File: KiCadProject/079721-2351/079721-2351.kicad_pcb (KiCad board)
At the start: 2 copper layers, 159.3 x 154.2 mm, 241 parts, among them IC1 HC244, IC101 uPC177C, IC201 MP493, IC401 D151811-0360, IC402 IS157, IC501 D151821-0020, IC601 MP5273, IC602 4071, IC603 4069, J201 Connected, J44 Conn_02x11_0x13_Top_Bottom_Sh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, J601 Connected, J711 Empty, Q802 C945, T1 2SB1015B, T211 RN1006, T711 2CS2001, T712 2SD1415, T721 2CS2001, T722 2SD1415, T751 CE1A3Q, T761 CE1A3Q, T801 2CS2001, T803 2CS4065, T811 2SC1815, T812 CE1A3Q, T821 Empty, T822 CE1A3Q (empty), T831 Empty, T832 CE1A3Q (empty), T841 2CS2001, T842 CE1A3Q, T851 Empty, T852 CE1A3Q (empty), T861 Empty, T911 RN1006, T921 RN1006, T921A1 Conn_01x01_Female, T921B1 Conn_01x01_Female, X601 Crystal

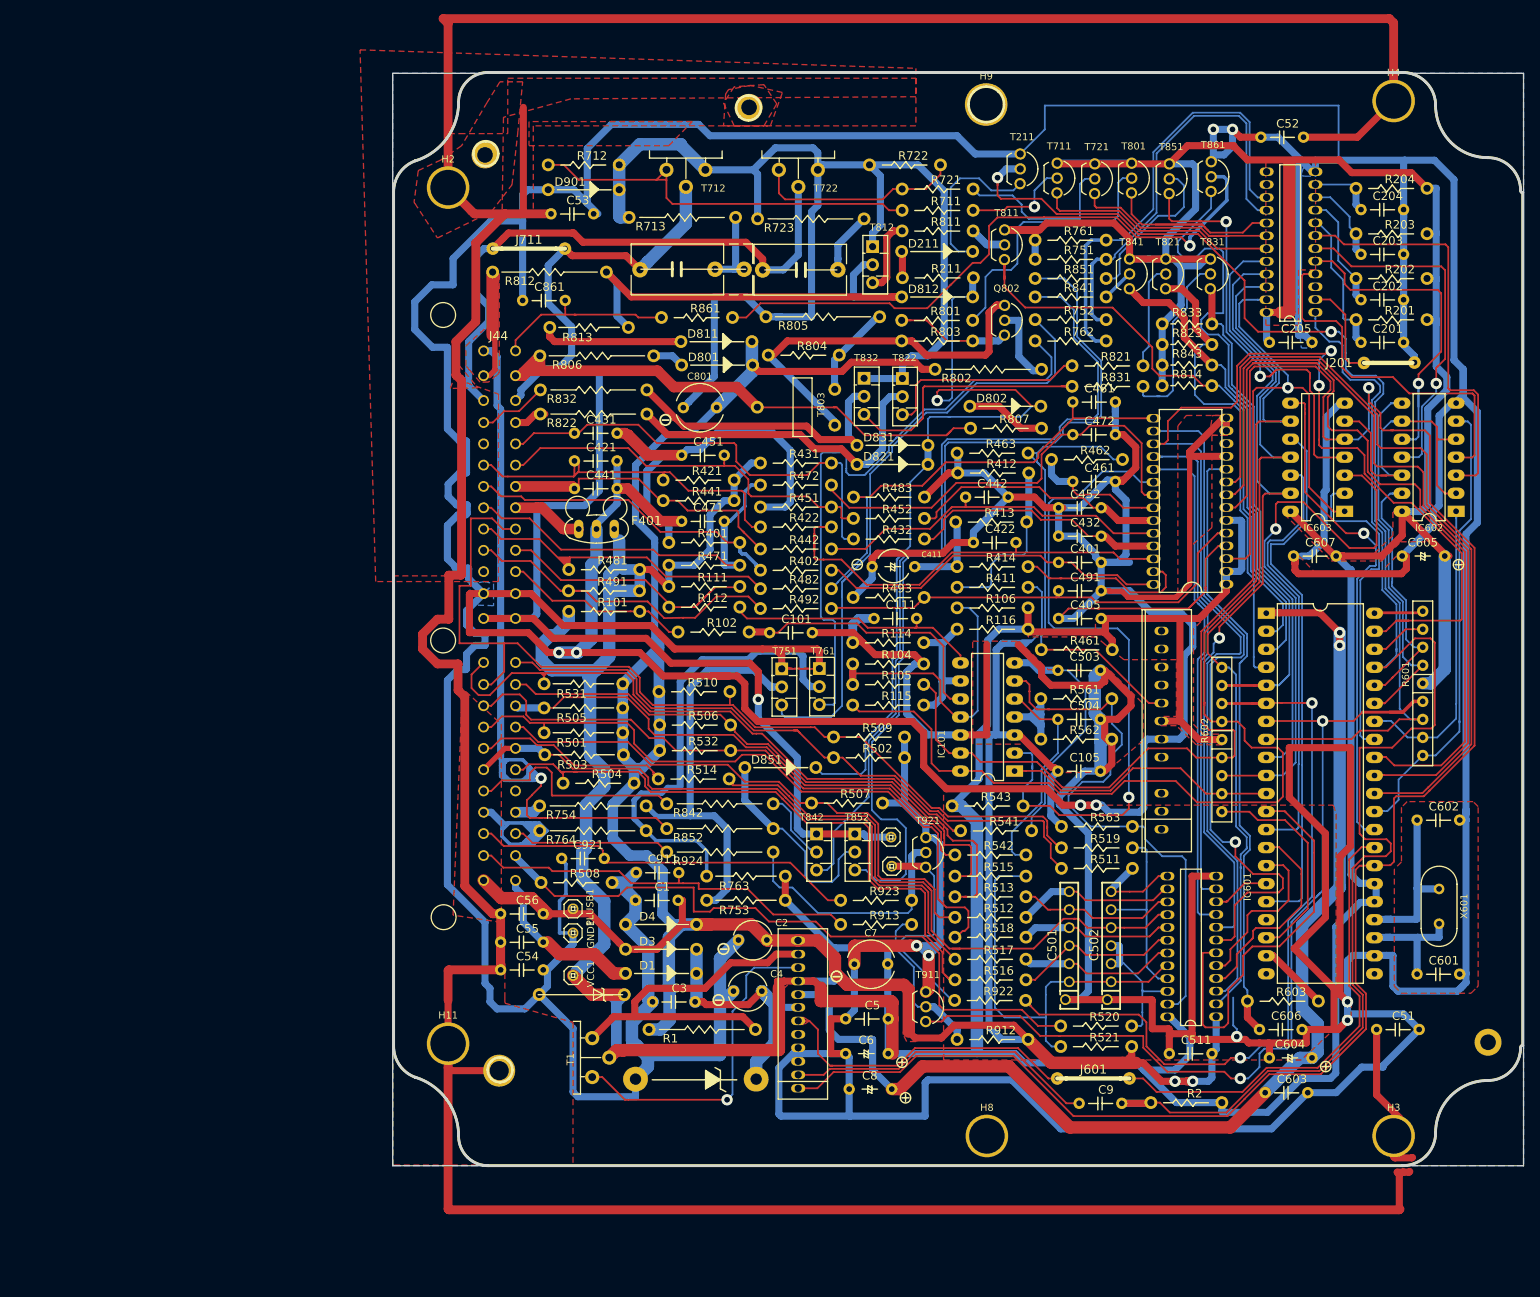
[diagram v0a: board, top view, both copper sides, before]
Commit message: 3D Models update
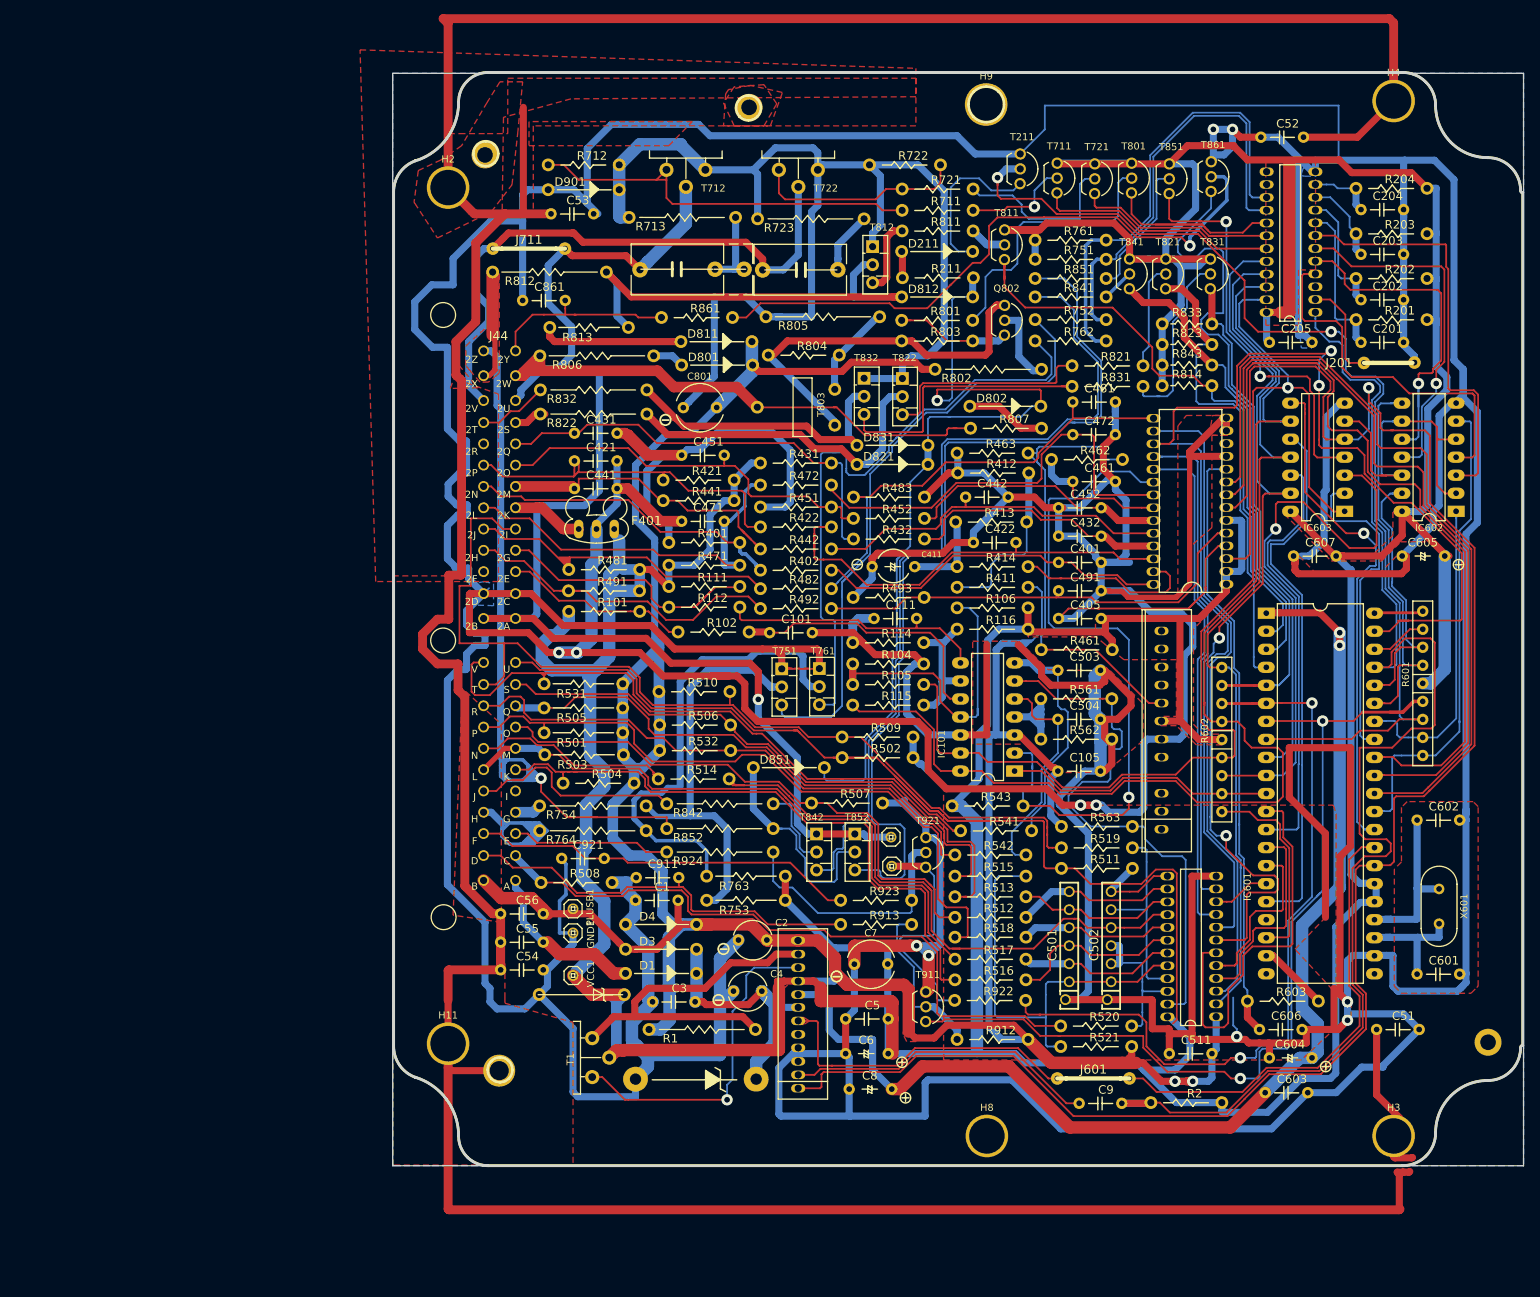
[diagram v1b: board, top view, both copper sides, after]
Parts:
- moved D851 1.20 mm to (131.7, 113.2)
- moved R502 1.20 mm to (144.2, 111.8)
- moved R509 1.20 mm to (144.2, 108.9)
- moved C911 0.70 mm to (111.2, 128.7)
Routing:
- net Headlight_switch: track 93.2 -> 166.3 mm
- net GNDS: track 1859.8 -> 1835.4 mm
- net IC601_12: track 58.6 -> 54.6 mm
- net IC601_37: track 55.2 -> 58.9 mm
- net Throttle_position_sensor: track 49.6 -> 52.8 mm
- net IC401_2: track 99.6 -> 96.6 mm
- net Transsmision_control_module: track 114.9 -> 111.9 mm
- net Net-(R851-Pad1): track 22.2 -> 19.4 mm
- net Net-(IC101-Pad11): track 44.7 -> 47.6 mm
- net Water_thermosensor: track 64.1 -> 61.3 mm
- net IC601_31: track 67.1 -> 69.8 mm
- net D851: track 119.3 -> 122.0 mm
- net Net-(IC603-Pad4): track 61.9 -> 59.3 mm
- net Net-(C503-Pad2): track 34.7 -> 32.1 mm
- net Net-(R831-Pad2): track 36.5 -> 39.1 mm
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
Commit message: Board shape
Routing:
- net GNDA: track 549.8 -> 492.1 mm
- net +5V: track 872.4 -> 877.3 mm
- net GNDS: track 1835.4 -> 1830.7 mm
- net Igniter_E: track 137.2 -> 133.5 mm
- net Neutral_or_clutch_switch: track 91.0 -> 94.3 mm
- net IC602_10: track 50.1 -> 52.9 mm
- net Net-(IC101-Pad11): track 47.6 -> 50.3 mm
- net Radiator_temperature_switch: track 79.0 -> 76.9 mm
- net EVAP_canister_purage_valve: track 17.3 -> 19.1 mm
- net IC601_41: track 192.3 -> 190.8 mm
- net IC601_5: track 102.2 -> 100.8 mm
- net /IC401_19: track 64.4 -> 65.7 mm
- net IC601_10: track 80.4 -> 81.6 mm
- net IC201_22: track 171.7 -> 170.5 mm
- net /IC401_10: track 51.9 -> 53.1 mm
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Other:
- board size 159.3 x 154.2 mm -> 159.9 x 153.4 mm
- board text added: "079721-2351"
- board text added: "2"
- board text added: "8"
- board text added: "91"
- board text added: "clone"
- board text removed: "Holes positions PCB shape"
- board text removed: "TODO"

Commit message: cleanup
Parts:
- moved T1 2.16 mm to (100.2, 158.4)
- moved R493 1.64 mm to (147.4, 89.2)
- moved R106 0.60 mm to (160.4, 91.3)
- moved D2 0.40 mm to (122.5, 157.1)
- moved C4 0.30 mm to (118.6, 144.7)
- moved R411 0.30 mm to (160.4, 87.5)
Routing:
- net GNDS: track 1830.7 -> 1896.2 mm
- net GNDA: track 492.1 -> 542.3 mm
- net Net-(R762-Pad2): track 87.2 -> 75.3 mm
- net +12V: track 415.6 -> 425.7 mm
- net Igniter_E: track 133.5 -> 141.8 mm
- net Self_diagnostic_checker_monitor_lamp: track 58.1 -> 65.8 mm
- net K: track 87.6 -> 93.6 mm
- net 2Y: track 26.6 -> 31.6 mm
- net Net-(R752-Pad2): track 91.2 -> 86.5 mm
- net Power_steering_pressure_switch: track 94.3 -> 98.5 mm
- net D851: track 122.0 -> 125.8 mm
- net +5V: track 877.3 -> 880.7 mm
- net Net-(IC402-Pad7): track 66.8 -> 63.7 mm
- net Volume_airflow_sensor: track 56.7 -> 59.9 mm
- net /IC401_10: track 53.1 -> 55.5 mm
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
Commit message: Cleanup
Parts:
- moved GND 38.6 mm to (59.0, 146.4)
- moved C201 38.5 mm to (176.0, 62.9)
- moved C202 38.5 mm to (176.0, 56.9)
- moved C203 38.5 mm to (176.0, 50.5)
- moved C204 38.5 mm to (176.0, 44.2)
- moved C205 38.5 mm to (163.1, 62.9)
- moved C721 38.5 mm to (91.1, 52.7)
- moved D831 38.5 mm to (109.0, 77.4)
- moved IC201 38.5 mm to (163.5, 58.7)
- moved IC601 38.5 mm to (156.7, 101.1)
- moved IC603 38.5 mm to (167.7, 86.7)
- moved R106 38.5 mm to (123.1, 100.9)
- moved R452 38.5 mm to (108.5, 87.7)
- moved R461 38.5 mm to (135.0, 106.2)
- moved R483 38.5 mm to (108.5, 84.7)
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- renumbered PLUSB1 to +B, C1 to C001, C2 to C002, C3 to C003, C4 to C004, C5 to C005, C6 to C006, C7 to C007, C8 to C008, C9 to C009, C51 to C051, C52 to C052, C53 to C053, C54 to C054, C55 to C055, C56 to C056, D1 to D001, D2 to D002, D3 to D003, D4 to D004, D5 to D005, GND1 to GND, IC1 to IC001, R1 to R001, R2 to R002, T1 to T001, VCC1 to VCC
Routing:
- net GNDS: track 1896.2 -> 1879.9 mm
- net Net-(R804-Pad1): track 13.9 -> 28.5 mm
- net Idle_air_control_valve: track 79.8 -> 71.3 mm
- net Injectors_1_3: track 54.5 -> 51.2 mm
- net 2S: track 4.63 -> 6.50 mm
- net Net-(D801-Pad2): track 4.48 -> 3.04 mm
- net +12V: track 425.7 -> 426.6 mm
- net 2T: track 10.3 -> 11.1 mm
- net Net-(Q802-Pad1): track 55.3 -> 56.0 mm
- net +BATT: track 23.1 -> 23.7 mm
- net Self_diagnostic_checker_monitor_lamp: track 65.8 -> 66.4 mm
- net Net-(D831-Pad2): track 42.0 -> 42.5 mm

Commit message: Board cleanup
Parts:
- renumbered C001 to C1, C002 to C2, C003 to C3, C004 to C4, C005 to C5, C051 to C51, C052 to C52, C053 to C53, C054 to C54, C055 to C55, C056 to C56, C006 to C6, C007 to C7, C008 to C8, C009 to C9, D001 to D1, D002 to D2, D003 to D3, D004 to D4, D005 to D5, GND to GND1, IC001 to IC1, +B to PLUSB1, R001 to R1, R002 to R2, T001 to T1, VCC to VCC1
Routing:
- net Headlight_switch: track 166.3 -> 126.7 mm
- net GNDS: track 1879.9 -> 1873.6 mm
- net /IC401_12: track 62.7 -> 59.4 mm
- net IC601_8: track 153.5 -> 155.5 mm
- net IC601_5: track 100.8 -> 99.2 mm
- net Transsmision_control_module: track 111.9 -> 110.9 mm
- net Net-(C101-Pad2): track 38.7 -> 39.5 mm
- net Stoplight_switch: track 86.9 -> 87.5 mm
- net Volume_airflow_sensor: track 59.9 -> 59.4 mm
